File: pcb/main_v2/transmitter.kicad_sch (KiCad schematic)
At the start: 24 parts, among them IC301 SE2576L-R, IC302 RMS-30+, J301 Conn_Coaxial, J302 Conn_Coaxial

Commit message: updated schematic after review
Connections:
- net CONN-3 renamed PA Enable
- net CONN-4 renamed PA DET Output
- net Carrier Frequency: Tx renamed Oscillator Tx
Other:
- note added: "f_c = 1.5 GHz"
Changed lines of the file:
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@@
+		)
+	)
+	(text "f_c = 1.5 GHz"
+		(exclude_from_sim no)
+		(at 129.032 150.876 0)
+		(effects
+			(font
+				(size 1.27 1.27)
+			)
 		)
 	)
@@
 	)
 	(junction
+		(at 90.17 73.66)
+		(diameter 0)
+		(color 0 0 0 0)
+	)
+	(junction
 		(at 232.41 73.66)
 		(diameter 0)
@@
 	)
 	(junction
-		(at 90.17 73.66)
+		(at 130.81 99.06)
 		(diameter 0)
 		(color 0 0 0 0)
@@
 	(junction
 		(at 191.77 73.66)
-		(diameter 0)
-		(color 0 0 0 0)
-	)
-	(junction
-		(at 130.81 99.06)
 		(diameter 0)
 		(color 0 0 0 0)
@@
 	(wire
 		(pts
+			(xy 69.85 73.66) (xy 90.17 73.66)
+		)
+		(stroke
+			(width 0)
+			(type default)
+		)
+	)
+	(wire
+		(pts
 			(xy 207.01 73.66) (xy 212.09 73.66)
 		)
@@
 	(wire
 		(pts
+			(xy 105.41 152.4) (xy 137.16 152.4)
+		)
+		(stroke
+			(width 0)
+			(type default)
+		)
+	)
+	(wire
+		(pts
 			(xy 49.53 157.48) (xy 52.07 157.48)
 		)
@@
 	(wire
 		(pts
-			(xy 77.47 73.66) (xy 90.17 73.66)
-		)
-		(stroke
-			(width 0)
-			(type default)
-		)
-	)
-	(wire
-		(pts
 			(xy 191.77 50.8) (xy 191.77 66.04)
 		)
@@
 	(wire
 		(pts
-			(xy 130.81 99.06) (xy 138.43 99.06)
+			(xy 130.81 99.06) (xy 148.59 99.06)
 		)
 		(stroke
@@
 		(pts
 			(xy 191.77 73.66) (xy 199.39 73.66)
-		)
-		(stroke
-			(width 0)
-			(type default)
-		)
-	)
-	(wire
-		(pts
-			(xy 111.76 152.4) (xy 105.41 152.4)
 		)
 		(stroke
@@
 		)
 	)
+	(label "f_antenne = 2.4 GHz"
+		(at 68.58 173.99 270)
+		(effects
+			(font
+				(size 1.27 1.27)
+			)
+			(justify right bottom)
+		)
+	)
 	(label "Filtered Tx"
 		(at 91.44 71.12 180)
@@
 		)
 	)
+	(label "https:{slash}{slash}www.eevblog.com{slash}forum{slash}rf-microwave{slash}2-4ghz-amplifier-quadrature-hybrid-coupler-balanced{slash}?action=dlattach;attach=686451"
+		(at 121.92 25.4 0)
+		(effects
+			(font
+				(size 1.27 1.27)
+			)
+			(justify left bottom)
+		)
+	)
 	(label "amplified Tx 2"
 		(at 246.38 73.66 270)
@@
 		)
 	)
+	(label "f_antenne = 2.4 GHz"
+		(at 259.08 68.58 0)
+		(effects
+			(font
+				(size 1.27 1.27)
+			)
+			(justify left bottom)
+		)
+	)
+	(label "f_sdr = 0.9 GHz"
+		(at 36.83 154.94 90)
+		(effects
+			(font
+				(size 1.27 1.27)
+			)
+			(justify left bottom)
+		)
+	)
 	(label "LO in"
 		(at 93.98 152.4 90)
@@
 		)
 	)
-	(global_label "CONN-3"
+	(hierarchical_label "PA Enable"
 		(shape input)
-		(at 77.47 73.66 270)
+		(at 69.85 73.66 180)
 		(fields_autoplaced yes)
 		(effects
@@
 			(justify right)
 		)
-		(property "Intersheetrefs" "${INTERSHEET_REFS}"
-			(at 77.47 84.6886 90)
-			(hide yes)
-			(show_name no)
-			(do_not_autoplace no)
-			(effects
-				(font
-					(size 1.27 1.27)
+		(property "Netzklasse" "Default"
+			(at 69.85 74.93 0)
+			(show_name no)
+			(do_not_autoplace no)
+			(effects
+				(font
+					(size 1.27 1.27)
+					(italic yes)
 				)
 				(justify right)
@@
 		)
 	)
-	(global_label "Carrier Frequency: Tx"
+	(hierarchical_label "PA DET Output"
 		(shape input)
-		(at 111.76 152.4 0)
+		(at 148.59 99.06 0)
 		(fields_autoplaced yes)
 		(effects
@@
 			(justify left)
 		)
-		(property "Intersheetrefs" "${INTERSHEET_REFS}"
-			(at 135.3071 152.4 0)
-			(hide yes)
-			(show_name no)
-			(do_not_autoplace no)
-			(effects
-				(font
-					(size 1.27 1.27)
+		(property "Netzklasse" "Default"
+			(at 148.59 100.33 0)
+			(show_name no)
+			(do_not_autoplace no)
+			(effects
+				(font
+					(size 1.27 1.27)
+					(italic yes)
 				)
 				(justify left)
@@
 		)
 	)
-	(global_label "CONN-4"
+	(hierarchical_label "Oscillator Tx"
 		(shape input)
-		(at 138.43 99.06 0)
+		(at 137.16 152.4 0)
 		(fields_autoplaced yes)
 		(effects
@@
 			(justify left)
 		)
-		(property "Intersheetrefs" "${INTERSHEET_REFS}"
-			(at 149.4586 99.06 0)
-			(hide yes)
-			(show_name no)
-			(do_not_autoplace no)
-			(effects
-				(font
-					(size 1.27 1.27)
+		(property "Netzklasse" "High Speed 50Ohm"
+			(at 137.16 153.67 0)
+			(show_name no)
+			(do_not_autoplace no)
+			(effects
+				(font
+					(size 1.27 1.27)
+					(italic yes)
 				)
 				(justify left)

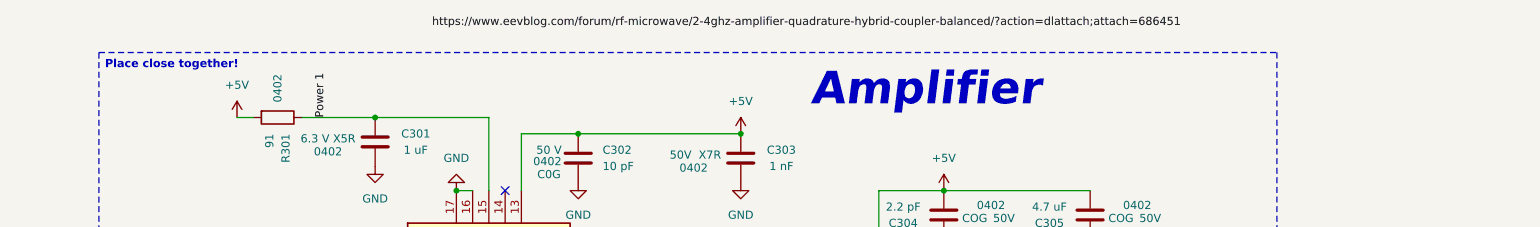
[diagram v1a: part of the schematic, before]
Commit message: added new osci
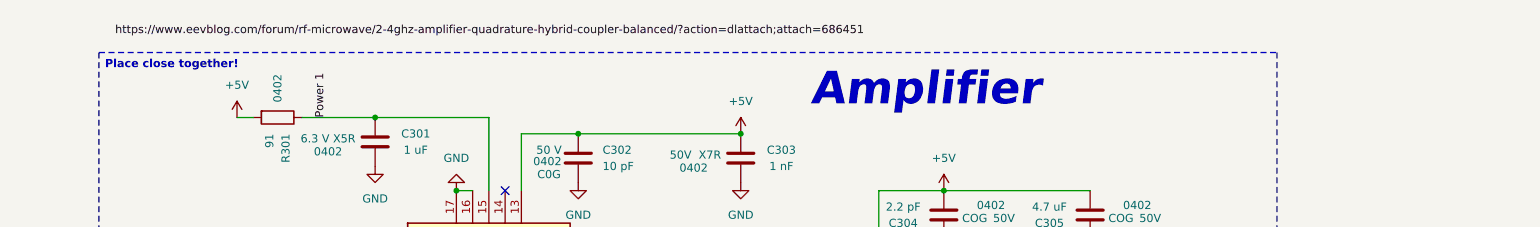
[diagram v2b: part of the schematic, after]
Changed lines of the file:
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@@
 	)
 	(label "https:{slash}{slash}www.eevblog.com{slash}forum{slash}rf-microwave{slash}2-4ghz-amplifier-quadrature-hybrid-coupler-balanced{slash}?action=dlattach;attach=686451"
-		(at 121.92 25.4 0)
+		(at 72.39 26.67 0)
 		(effects
 			(font

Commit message: updated pll
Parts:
- D301: footprint LED_SMD:LED_0603_1608Metric -> LED_SMD:LED_0805_2012Metric
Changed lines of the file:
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@@
 			)
 		)
-		(property "Footprint" "LED_SMD:LED_0603_1608Metric"
+		(property "Footprint" "LED_SMD:LED_0805_2012Metric"
 			(at 90.17 81.28 0)
 			(hide yes)

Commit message: updarted schematic and simulation
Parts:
- removed J301, J302: Conn_Coaxial, Connector_Coaxial:SMA_Amphenol_132289_EdgeMount, symbol Connector:Conn_Coaxial
- C313, C314: value 10 pF -> 100 pF
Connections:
- net LO in: no longer names the net of C312.1, IC302.1 (LO)
- net Power 1: no longer names the net of C301.2, IC301.15 (VCC1), R301.1
- net Tx In 1: no longer names the net of C313.2, IC302.5 (IF)
- net Upconverted: no longer names the net of C314.1, IC302.4 (RF)
- net Upconverted 1: no longer names the net of C314.2, FL301.1 (IN/OUT)
- net amplified Tx: no longer names the net of C306.1, C308.1, C309.1, IC301.10 (RFOUT), IC301.11 (RF_OUT), R302.2
- net amplified Tx 1: no longer names the net of C306.2, L301.2
- net amplified Tx 2 renamed Tx Out
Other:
- note added: "alternive power attenuatoren mit dip schalter: PE4312"
- note removed: "Tx In ->"
- note removed: "Tx Out ->"
- note removed: "f_c = 1.5 GHz"
- moved on the sheet: C301, C302, C303, C304, C305, C306, C307, C308, C309, C310, D301, IC301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

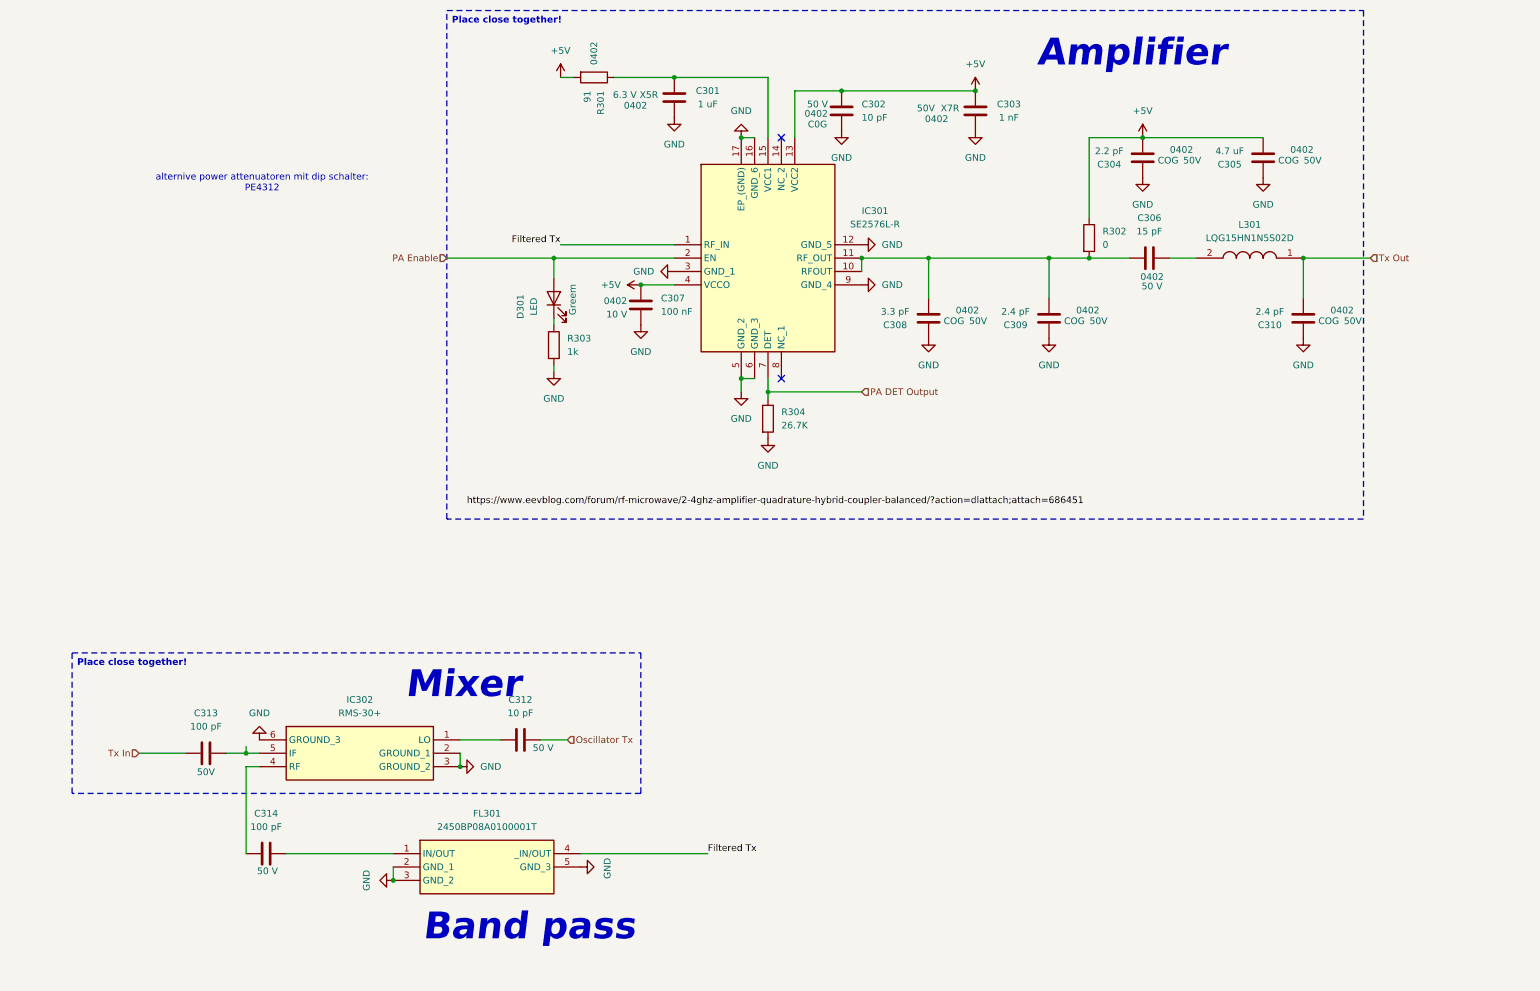
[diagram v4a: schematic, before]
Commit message: updated io schematic
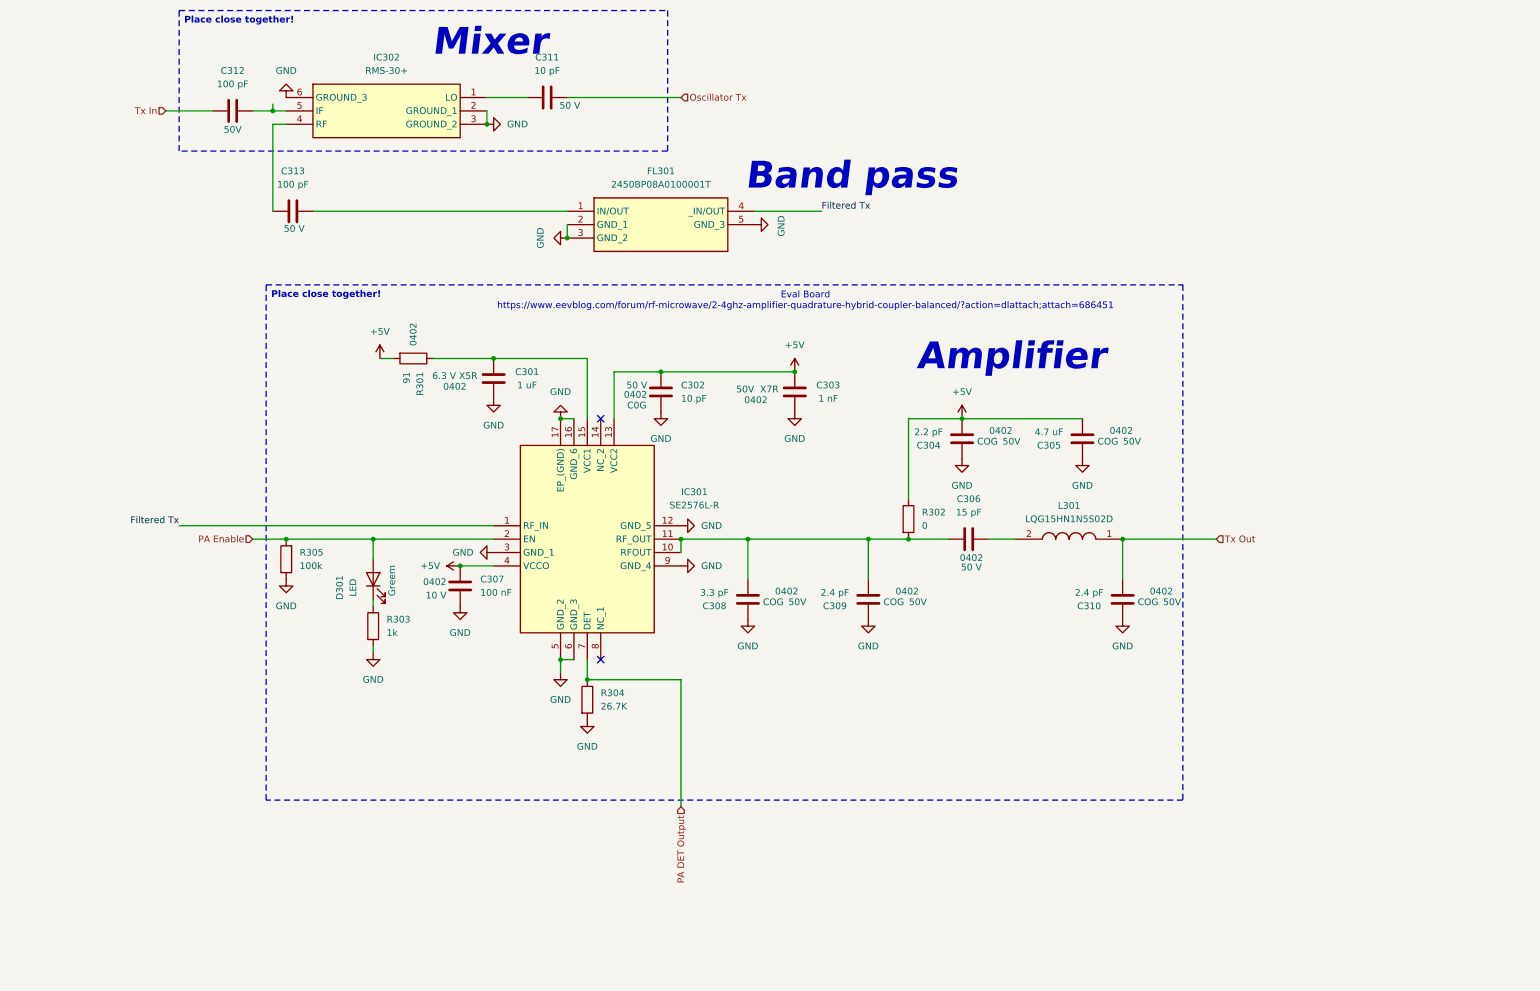
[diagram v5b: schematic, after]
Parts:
- added R305: 100k, Resistor_SMD:R_0603_1608Metric, symbol Device:R
- renumbered C312 to C311, C313 to C312, C314 to C313
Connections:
- net GND: now also R305.1
- net PA Enable: now also R305.2
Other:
- note added: "Eval Board https://www.eevblog.com/forum/rf-microwave/2-4ghz-amplifier-quadrature-hybrid-coupler-balanced/?action=dlattach;attach=686451"
- note removed: "alternive power attenuatoren mit dip schalter: PE4312"
- moved on the sheet: C301, C302, C303, C304, C305, C306, C307, C308, C309, C310, C311, C312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

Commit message: update bom
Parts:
- removed C313: 100 pF, Capacitor_SMD:C_0402_1005Metric, symbol Device:C
- removed R304: 26.7K, Resistor_SMD:R_0603_1608Metric, symbol Device:R
- added C303: 100 pF, Capacitor_SMD:C_0402_1005Metric, symbol Device:C
- added R305: 26.7K, Resistor_SMD:R_0603_1608Metric, symbol Device:R
- renumbered C311 to C301, C312 to C302, C301 to C304, C302 to C305, C303 to C306, C304 to C307, C305 to C308, C306 to C309, C307 to C310, C308 to C311, C309 to C312, C310 to C313, IC302 to IC301, IC301 to IC302, R305 to R303, R303 to R304
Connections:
- net GND: now also R305.2
- net PA DET Output: now also R305.1
- net RF Out: now reaches FL301.1 (IN/OUT)
- net RF Out: now also C303.2
- net at IC301.4 (RF): now also C303.1
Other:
- moved on the sheet: C304, C305, C306, C307, C308, C309, C310, C311, C312, C313, D301, FL301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

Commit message: updated layout
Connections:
- net +5V: now also R301.1; no longer R301.2
- net at C304.2, IC302.15 (VCC1): now also R301.2; no longer R301.1
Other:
- moved on the sheet: R301
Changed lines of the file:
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@@
 	(symbol
 		(lib_id "Device:R")
-		(at 69.85 76.2 270)
+		(at 69.85 76.2 90)
 		(unit 1)
 		(body_style 1)
@@
 		(dnp no)
 		(property "Reference" "R301"
-			(at 71.1201 78.74 0)
+			(at 68.5799 73.66 0)
 			(show_name no)
 			(do_not_autoplace no)
@@
 		)
 		(property "Value" "91"
-			(at 68.5801 78.74 0)
+			(at 71.1199 73.66 0)
 			(show_name no)
 			(do_not_autoplace no)
@@
 		)
 		(property "Footprint" "Resistor_SMD:R_0402_1005Metric"
-			(at 69.85 74.422 90)
+			(at 69.85 77.978 90)
 			(hide yes)
 			(show_name no)
@@
 		)
 		(property "Package" "0402 "
-			(at 69.85 71.628 0)
+			(at 69.85 80.772 0)
 			(show_name no)
 			(do_not_autoplace no)
@@
 		(lib_id "Device:C")
 		(at 78.74 119.38 0)
+		(mirror y)
 		(unit 1)
 		(body_style 1)
@@
 		(dnp no)
 		(property "Reference" "C310"
-			(at 82.55 118.1099 0)
+			(at 74.93 118.1099 0)
 			(show_name no)
 			(do_not_autoplace no)
@@
 		)
 		(property "Value" "100 nF"
-			(at 82.55 120.6499 0)
+			(at 74.93 120.6499 0)
 			(show_name no)
 			(do_not_autoplace no)
@@
 		)
 		(property "Footprint" "Capacitor_SMD:C_0402_1005Metric"
-			(at 79.7052 123.19 0)
+			(at 77.7748 123.19 0)
 			(hide yes)
 			(show_name no)
@@
 		)
 		(property "Package" "0402"
-			(at 73.914 118.618 0)
+			(at 83.566 118.618 0)
 			(show_name no)
 			(do_not_autoplace no)
@@
 		)
 		(property "Voltage" "10 V"
-			(at 74.168 121.158 0)
-			(show_name no)
-			(do_not_autoplace no)
+			(at 83.312 121.158 0)
+			(show_name no)
+			(do_not_autoplace no)
